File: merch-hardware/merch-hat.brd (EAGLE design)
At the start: 65 x 56 mm, 15 parts

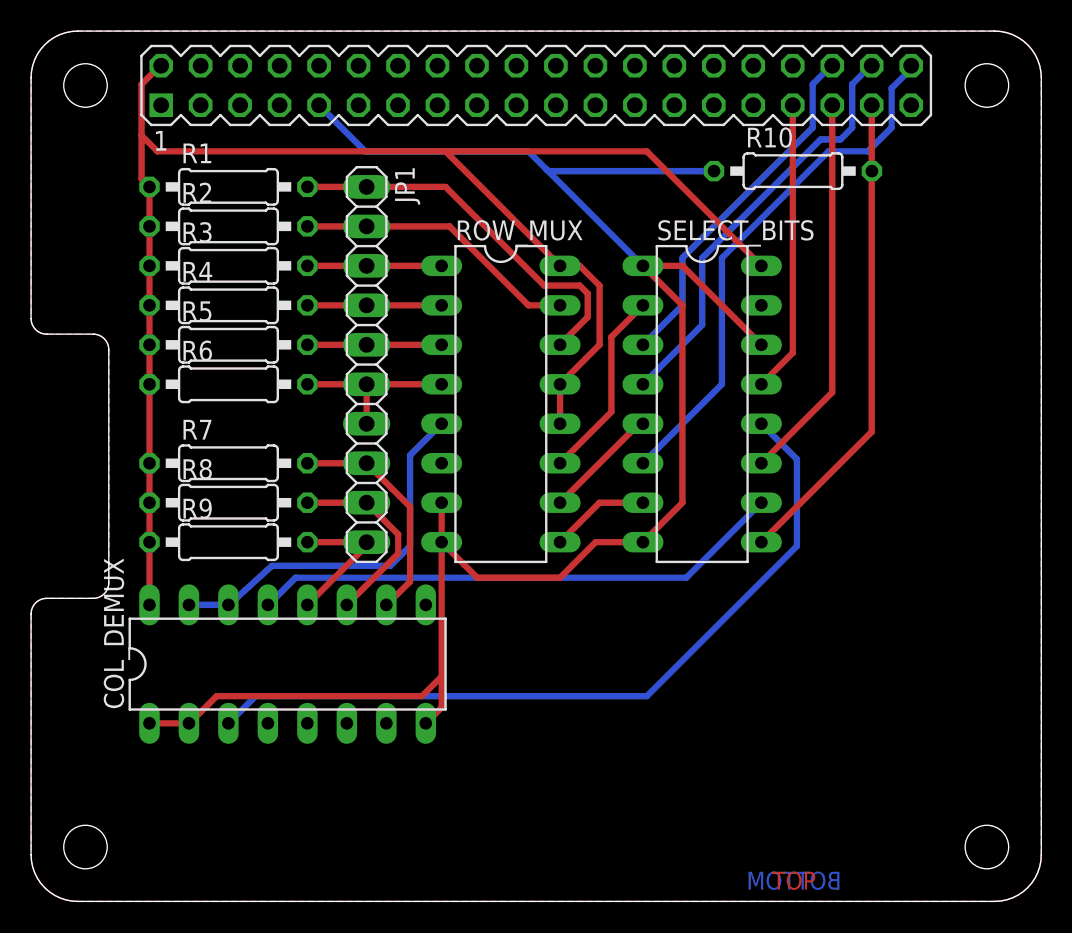
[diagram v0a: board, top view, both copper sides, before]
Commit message: Moved some silkscreen, fixed DRU issue
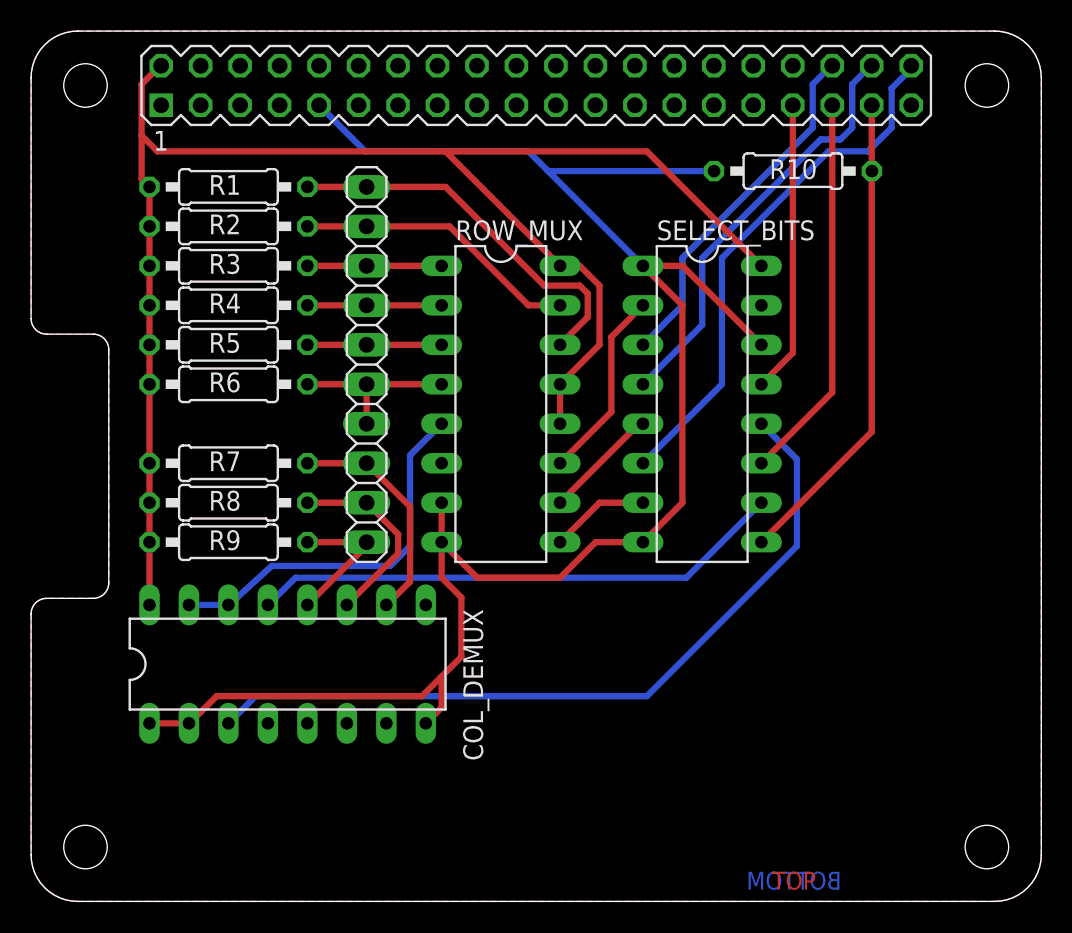
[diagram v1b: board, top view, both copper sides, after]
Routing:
- net GND: track 115.1 -> 116.0 mm
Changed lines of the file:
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@@
 <?xml version="1.0" encoding="utf-8"?>
 <!DOCTYPE eagle SYSTEM "eagle.dtd">
-<eagle version="8.0.1">
+<eagle version="7.6.0">
 <drawing>
 <settings>
@@
 <layer number="18" name="Vias" color="2" fill="1" visible="yes" active="yes"/>
 <layer number="19" name="Unrouted" color="6" fill="1" visible="yes" active="yes"/>
-<layer number="20" name="Dimension" color="15" fill="1" visible="no" active="yes"/>
+<layer number="20" name="Dimension" color="15" fill="1" visible="yes" active="yes"/>
 <layer number="21" name="tPlace" color="7" fill="1" visible="yes" active="yes"/>
 <layer number="22" name="bPlace" color="7" fill="1" visible="yes" active="yes"/>
@@
 </class>
 </classes>
-<designrules name="ITEADstudio_DRC">
+<designrules name="SeeedStudio_2layer_DRU_no_angle_20140221">
+<description language="de">&lt;b&gt;EAGLE Design Rules&lt;/b&gt;
+&lt;p&gt;
+Die Standard-Design-Rules sind so gewählt, dass sie für
+die meisten Anwendungen passen. Sollte ihre Platine
+besondere Anforderungen haben, treffen Sie die erforderlichen
+Einstellungen hier und speichern die Design Rules unter
+einem neuen Namen ab.</description>
 <description language="en">&lt;b&gt;EAGLE Design Rules&lt;/b&gt;
 &lt;p&gt;
@@
 necessary adjustments and save your customized
 design rules under a new name.</description>
+<description language="zh">&lt;b&gt;Seeed Studio EAGLE Design Rules&lt;/b&gt;
+</description>
 <param name="layerSetup" value="(1*16)"/>
-<param name="mtCopper" value="0.035mm 0.035mm 0.035mm 0.035mm 0.035mm 0.035mm 0.035mm 0.035mm 0.035mm 0.035mm 0.035mm 0.035mm 0.035mm 0.035mm 0.035mm 0.035mm"/>
-<param name="mtIsolate" value="1.5mm 0.15mm 0.2mm 0.15mm 0.2mm 0.15mm 0.2mm 0.15mm 0.2mm 0.15mm 0.2mm 0.15mm 0.2mm 0.15mm 0.2mm"/>
+<param name="mtCopper" value="0.035mm 0.0175mm 0.035mm 0.035mm 0.035mm 0.035mm 0.035mm 0.035mm 0.035mm 0.035mm 0.035mm 0.035mm 0.035mm 0.035mm 0.0175mm 0.035mm"/>
+<param name="mtIsolate" value="1.5mm 1.1mm 0.2mm 0.15mm 0.2mm 0.15mm 0.2mm 0.15mm 0.2mm 0.15mm 0.2mm 0.15mm 0.2mm 0.15mm 0.2mm"/>
 <param name="mdWireWire" value="6mil"/>
 <param name="mdWirePad" value="6mil"/>
@@
 <elements>
 <element name="GPIO" library="FLYFISH" package="PIN_20X2" value="PIN20X2" x="32.5" y="52.5" smashed="yes">
-<attribute name="VALUE" x="45.2" y="48.309" size="1.27" layer="27" ratio="10"/>
+<attribute name="VALUE" x="37.58" y="48.309" size="1.27" layer="27" ratio="10"/>
 </element>
 <element name="ROW_MUX" library="74xx-us" package="DIL16" value="74LS151N" x="30.226" y="32.004" rot="R270"/>
-<element name="COL_DEMUX" library="74xx-us" package="DIL16" value="74LS155N" x="16.508" y="15.27"/>
+<element name="COL_DEMUX" library="74xx-us" package="DIL16" value="74LS155N" x="16.508" y="15.27" smashed="yes">
+<attribute name="NAME" x="29.081" y="9.047" size="1.27" layer="25" ratio="10" rot="R90"/>
+<attribute name="VALUE" x="9.015" y="14.635" size="1.27" layer="27" ratio="10"/>
+</element>
 <element name="SELECT_BITS" library="74xx-us" package="DIL16" value="74LS174N" x="43.18" y="32.004" rot="R270"/>
-<element name="JP1" library="pinhead" package="1X10" value="HEADER" x="21.59" y="34.544" rot="R270"/>
-<element name="R1" library="resistor" package="0207/10" value="3.3k" x="12.7" y="45.974"/>
-<element name="R2" library="resistor" package="0207/10" value="3.3k" x="12.7" y="43.434"/>
-<element name="R3" library="resistor" package="0207/10" value="3.3k" x="12.7" y="40.894"/>
-<element name="R4" library="resistor" package="0207/10" value="3.3k" x="12.7" y="38.354"/>
-<element name="R5" library="resistor" package="0207/10" value="3.3k" x="12.7" y="35.814"/>
-<element name="R6" library="resistor" package="0207/10" value="3.3k" x="12.7" y="33.274"/>
-<element name="R7" library="resistor" package="0207/10" value="3.3k" x="12.7" y="28.194"/>
-<element name="R8" library="resistor" package="0207/10" value="3.3k" x="12.7" y="25.654"/>
-<element name="R9" library="resistor" package="0207/10" value="3.3k" x="12.7" y="23.114"/>
-<element name="R10" library="resistor" package="0207/10" value="3.3k" x="49.022" y="46.99"/>
+<element name="JP1" library="pinhead" package="1X10" value="HEADER" x="21.59" y="34.544" smashed="yes" rot="R270">
+<attribute name="VALUE" x="18.415" y="47.244" size="1.27" layer="27" rot="R270"/>
+</element>
+<element name="R1" library="resistor" package="0207/10" value="3.3k" x="12.7" y="45.974" smashed="yes">
+<attribute name="NAME" x="11.43" y="45.466" size="1.27" layer="25" ratio="10"/>
+<attribute name="VALUE" x="10.4394" y="45.339" size="1.27" layer="27" ratio="10"/>
+</element>
+<element name="R2" library="resistor" package="0207/10" value="3.3k" x="12.7" y="43.434" smashed="yes">
+<attribute name="NAME" x="11.43" y="42.926" size="1.27" layer="25" ratio="10"/>
+<attribute name="VALUE" x="10.4394" y="42.799" size="1.27" layer="27" ratio="10"/>
+</element>
+<element name="R3" library="resistor" package="0207/10" value="3.3k" x="12.7" y="40.894" smashed="yes">
+<attribute name="NAME" x="11.43" y="40.386" size="1.27" layer="25" ratio="10"/>
+<attribute name="VALUE" x="10.4394" y="40.259" size="1.27" layer="27" ratio="10"/>
+</element>
+<element name="R4" library="resistor" package="0207/10" value="3.3k" x="12.7" y="38.354" smashed="yes">
+<attribute name="NAME" x="11.43" y="37.846" size="1.27" layer="25" ratio="10"/>
+<attribute name="VALUE" x="10.4394" y="37.719" size="1.27" layer="27" ratio="10"/>
+</element>
+<element name="R5" library="resistor" package="0207/10" value="3.3k" x="12.7" y="35.814" smashed="yes">
+<attribute name="NAME" x="11.43" y="35.306" size="1.27" layer="25" ratio="10"/>
+<attribute name="VALUE" x="10.4394" y="35.179" size="1.27" layer="27" ratio="10"/>
+</element>
+<element name="R6" library="resistor" package="0207/10" value="3.3k" x="12.7" y="33.274" smashed="yes">
+<attribute name="NAME" x="11.43" y="32.766" size="1.27" layer="25" ratio="10"/>
+<attribute name="VALUE" x="10.4394" y="32.639" size="1.27" layer="27" ratio="10"/>
+</element>
+<element name="R7" library="resistor" package="0207/10" value="3.3k" x="12.7" y="28.194" smashed="yes">
+<attribute name="NAME" x="11.43" y="27.686" size="1.27" layer="25" ratio="10"/>
+<attribute name="VALUE" x="10.4394" y="27.559" size="1.27" layer="27" ratio="10"/>
+</element>
+<element name="R8" library="resistor" package="0207/10" value="3.3k" x="12.7" y="25.654" smashed="yes">
+<attribute name="NAME" x="11.43" y="25.146" size="1.27" layer="25" ratio="10"/>
+<attribute name="VALUE" x="10.4394" y="25.019" size="1.27" layer="27" ratio="10"/>
+</element>
+<element name="R9" library="resistor" package="0207/10" value="3.3k" x="12.7" y="23.114" smashed="yes">
+<attribute name="NAME" x="11.43" y="22.606" size="1.27" layer="25" ratio="10"/>
+<attribute name="VALUE" x="10.4394" y="22.479" size="1.27" layer="27" ratio="10"/>
+</element>
+<element name="R10" library="resistor" package="0207/10" value="3.3k" x="49.022" y="46.99" smashed="yes">
+<attribute name="NAME" x="47.498" y="46.482" size="1.27" layer="25" ratio="10"/>
+<attribute name="VALUE" x="46.7614" y="46.355" size="1.27" layer="27" ratio="10"/>
+</element>
 </elements>
 <signals>
@@
 <contactref element="COL_DEMUX" pad="1"/>
 <contactref element="GPIO" pad="9"/>
-<wire x1="26.416" y1="23.114" x2="26.416" y2="14.478" width="0.4064" layer="1"/>
 <wire x1="26.416" y1="14.478" x2="26.416" y2="12.478" width="0.4064" layer="1"/>
 <wire x1="26.416" y1="12.478" x2="25.398" y2="11.46" width="0.4064" layer="1"/>
@@
 <wire x1="41.91" y1="38.354" x2="41.91" y2="25.654" width="0.4064" layer="1"/>
 <wire x1="41.91" y1="25.654" x2="39.37" y2="23.114" width="0.4064" layer="1"/>
-<wire x1="33.147" y1="47.117" x2="39.37" y2="40.894" width="0.4064" layer="16"/>
+<wire x1="33.274" y1="46.99" x2="39.37" y2="40.894" width="0.4064" layer="16"/>
 <wire x1="33.147" y1="47.117" x2="32.004" y2="48.26" width="0.4064" layer="16"/>
 <wire x1="32.004" y1="48.26" x2="21.5" y2="48.26" width="0.4064" layer="16"/>
@@
 <wire x1="43.942" y1="46.99" x2="33.274" y2="46.99" width="0.4064" layer="16"/>
 <wire x1="33.274" y1="46.99" x2="33.147" y2="47.117" width="0.4064" layer="16"/>
+<wire x1="26.416" y1="23.114" x2="26.416" y2="20.828" width="0.4064" layer="1"/>
+<wire x1="26.416" y1="20.828" x2="27.686" y2="19.558" width="0.4064" layer="1"/>
+<wire x1="27.686" y1="19.558" x2="27.686" y2="15.748" width="0.4064" layer="1"/>
+<wire x1="27.686" y1="15.748" x2="26.416" y2="14.478" width="0.4064" layer="1"/>
 </signal>
 <signal name="+5V">
@@
 <wire x1="21.59" y1="23.114" x2="21.59" y2="22.892" width="0.4064" layer="1"/>
 <wire x1="21.59" y1="22.892" x2="17.778" y2="19.08" width="0.4064" layer="1"/>
-<wire x1="17.78" y1="23.114" x2="17.78" y2="23.114" width="0" layer="19" extent="1-16"/>
 </signal>
 <signal name="N$12">
